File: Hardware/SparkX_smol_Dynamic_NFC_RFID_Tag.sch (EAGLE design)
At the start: 22 parts, among them U1 ST25DV64KC

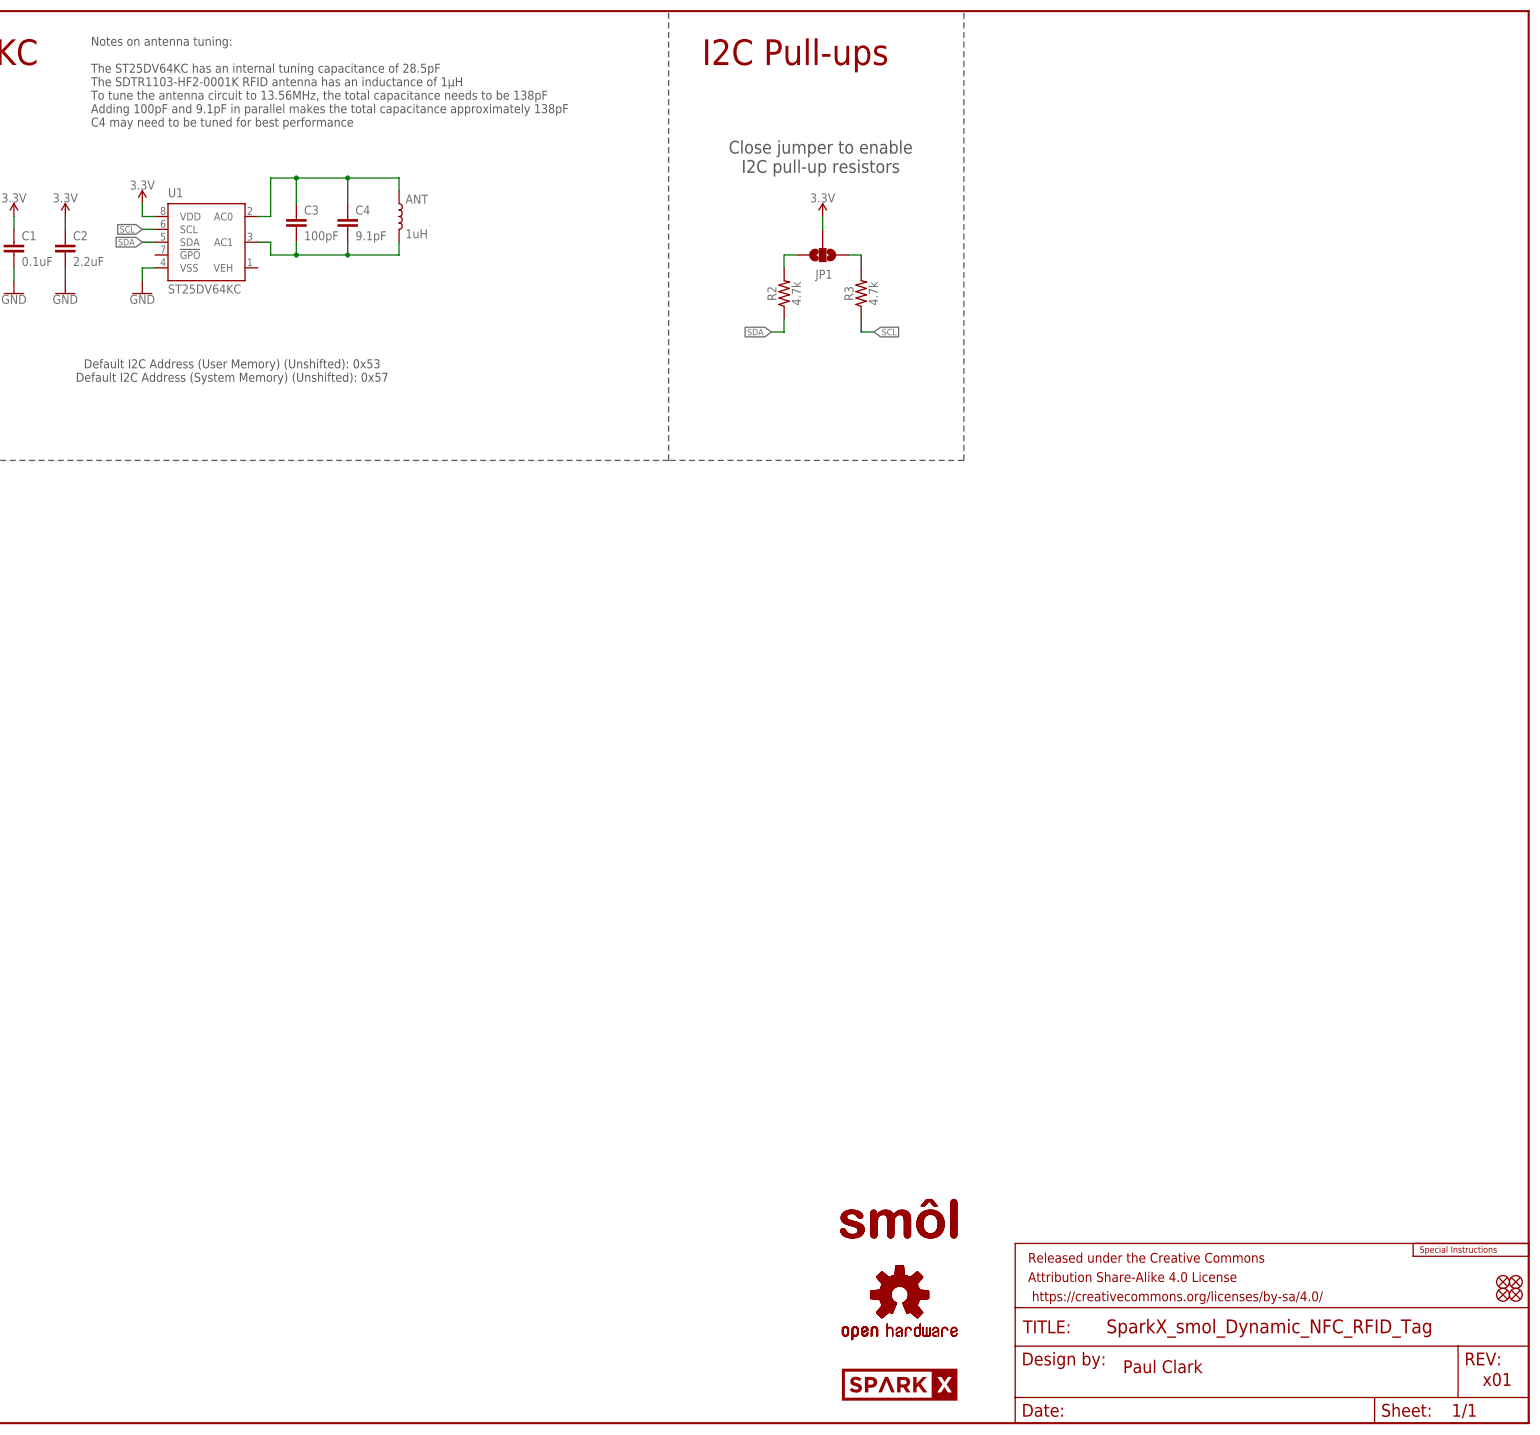
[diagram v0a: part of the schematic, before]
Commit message: x02: change to W3102 antenna
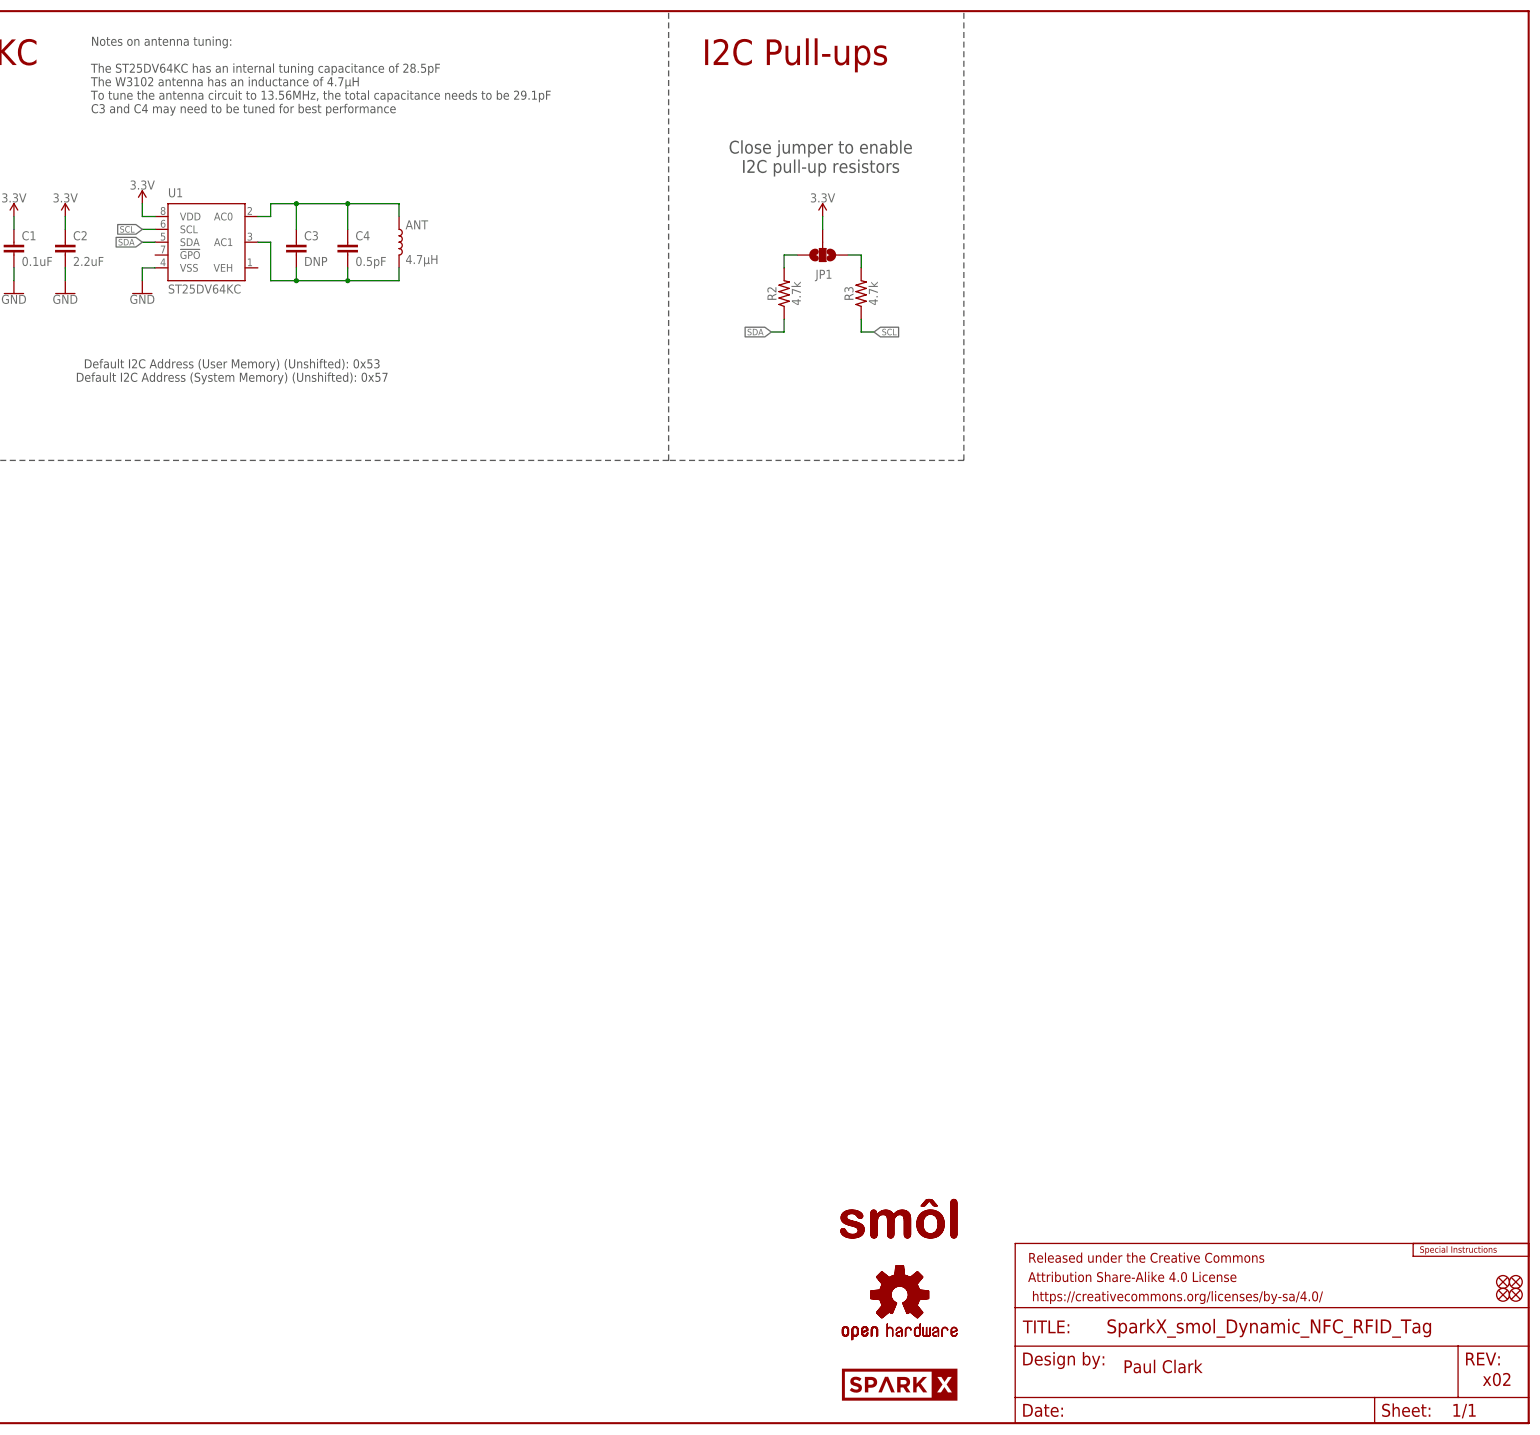
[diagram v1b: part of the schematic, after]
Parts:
- ANT: value 1uH -> 4.7μH; device SparkFun-RF:RFID_ANTENNA_SDTR1103-HF2-1UH -> SparkFun-RF:RFID_ANTENNA_W3102
- C3: value 100pF -> DNP; device SparkFun-Capacitors:100PF-0402T-50V-5% -> SparkFun-Capacitors:DNP-0402-TIGHT_NO_CREAM
- C4: value 9.1pF -> 0.5pF; device SparkFun-Capacitors:9.1PF-0402-TIGHT -> SparkFun-Capacitors:0.5PF-0402_TIGHT-50V-PM0.05PF-NP0
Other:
- note added: "Notes on antenna tuning: The ST25DV64KC has an internal tuning capacitance of 28.5pF The W3102 antenna has an inductance of 4.7µH To tune the antenna circuit to 13.56MHz, the total capacitance needs to be 29.1pF C3 and C4 may need to be tuned for best performance"
- note added: "x02"
- note removed: "Notes on antenna tuning: The ST25DV64KC has an internal tuning capacitance of 28.5pF The SDTR1103-HF2-0001K RFID antenna has an inductance of 1µH To tune the antenna circuit to 13.56MHz, the total capacitance needs to be 138pF Adding 100pF and 9.1pF in parallel makes the total capacitance approximately 138pF C4 may need to be tuned for best performance"
- note removed: "x01"
- moved on the sheet: ANT, C3, C4
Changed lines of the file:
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@@
 <part name="SUPPLY2" library="SparkFun-PowerSymbols" deviceset="3.3V" device=""/>
 <part name="GND2" library="SparkFun-PowerSymbols" deviceset="GND" device=""/>
-<part name="C3" library="SparkFun-Capacitors" deviceset="100PF" device="-0402T-50V-5%" value="100pF"/>
-<part name="C4" library="SparkFun-Capacitors" deviceset="9.1PF" device="-0402-TIGHT" value="9.1pF"/>
-<part name="ANT" library="SparkFun-RF" deviceset="RFID_ANTENNA_SDTR1103-HF2" device="-1UH" value="1uH"/>
+<part name="C3" library="SparkFun-Capacitors" deviceset="DNP" device="-0402-TIGHT_NO_CREAM" value="DNP"/>
+<part name="C4" library="SparkFun-Capacitors" deviceset="0.5PF" device="-0402_TIGHT-50V-PM0.05PF-NP0" value="0.5pF"/>
+<part name="ANT" library="SparkFun-RF" deviceset="RFID_ANTENNA_W3102" device="" value="4.7μH"/>
 <part name="R2" library="SparkFun-Resistors" deviceset="4.7KOHM" device="-0402T-1/16W-1%" value="4.7k"/>
 <part name="R3" library="SparkFun-Resistors" deviceset="4.7KOHM" device="-0402T-1/16W-1%" value="4.7k"/>
@@
 <plain>
 <text x="351.536" y="9.906" size="2.54" layer="94">Paul Clark</text>
-<text x="422.656" y="7.366" size="2.54" layer="94">x01</text>
+<text x="422.656" y="7.366" size="2.54" layer="94">x02</text>
 <wire x1="88.9" y1="190.5" x2="88.9" y2="279.4" width="0.2032" layer="97" style="longdash"/>
 <wire x1="88.9" y1="190.5" x2="0" y2="190.5" width="0.2032" layer="97" style="longdash"/>
@@
 <text x="147.32" y="274.32" size="1.778" layer="97" align="top-left">Notes on antenna tuning:
 The ST25DV64KC has an internal tuning capacitance of 28.5pF
-The SDTR1103-HF2-0001K RFID antenna has an inductance of 1µH
-To tune the antenna circuit to 13.56MHz, the total capacitance needs to be 138pF
-Adding 100pF and 9.1pF in parallel makes the total capacitance approximately 138pF
-C4 may need to be tuned for best performance</text>
+The W3102 antenna has an inductance of 4.7µH
+To tune the antenna circuit to 13.56MHz, the total capacitance needs to be 29.1pF
+C3 and C4 may need to be tuned for best performance</text>
 <text x="291.719" y="250.571" size="2.54" layer="97" font="vector" align="center">Close jumper to enable
 I2C pull-up resistors</text>
@@
 <attribute name="VALUE" x="132.08" y="223.266" size="1.778" layer="96" font="vector" align="top-center"/>
 </instance>
-<instance part="C3" gate="G$1" x="187.96" y="236.22" smashed="yes">
-<attribute name="NAME" x="189.484" y="239.141" size="1.778" layer="95" font="vector"/>
-<attribute name="VALUE" x="189.484" y="234.061" size="1.778" layer="96" font="vector"/>
-</instance>
-<instance part="C4" gate="G$1" x="198.12" y="236.22" smashed="yes">
-<attribute name="NAME" x="199.644" y="239.141" size="1.778" layer="95" font="vector"/>
-<attribute name="VALUE" x="199.644" y="234.061" size="1.778" layer="96" font="vector"/>
-</instance>
-<instance part="ANT" gate="G$1" x="208.28" y="238.76" smashed="yes">
-<attribute name="NAME" x="209.55" y="241.3" size="1.778" layer="95" font="vector"/>
-<attribute name="VALUE" x="209.55" y="236.22" size="1.778" layer="96" font="vector" align="top-left"/>
+<instance part="C3" gate="G$1" x="187.96" y="231.14" smashed="yes">
+<attribute name="NAME" x="189.484" y="234.061" size="1.778" layer="95" font="vector"/>
+<attribute name="VALUE" x="189.484" y="228.981" size="1.778" layer="96" font="vector"/>
+</instance>
+<instance part="C4" gate="G$1" x="198.12" y="231.14" smashed="yes">
+<attribute name="NAME" x="199.644" y="234.061" size="1.778" layer="95" font="vector"/>
+<attribute name="VALUE" x="199.644" y="228.981" size="1.778" layer="96" font="vector"/>
+</instance>
+<instance part="ANT" gate="G$1" x="208.28" y="233.68" smashed="yes">
+<attribute name="NAME" x="209.55" y="236.22" size="1.778" layer="95" font="vector"/>
+<attribute name="VALUE" x="209.55" y="231.14" size="1.778" layer="96" font="vector" align="top-left"/>
 </instance>
 <instance part="R2" gate="G$1" x="284.48" y="223.52" smashed="yes" rot="R90">
@@
 <pinref part="U1" gate="G$1" pin="AC1"/>
 <wire x1="180.34" y1="233.68" x2="182.88" y2="233.68" width="0.1524" layer="91"/>
-<wire x1="182.88" y1="233.68" x2="182.88" y2="231.14" width="0.1524" layer="91"/>
-<wire x1="182.88" y1="231.14" x2="187.96" y2="231.14" width="0.1524" layer="91"/>
+<wire x1="182.88" y1="233.68" x2="182.88" y2="226.06" width="0.1524" layer="91"/>
+<wire x1="182.88" y1="226.06" x2="187.96" y2="226.06" width="0.1524" layer="91"/>
 <pinref part="ANT" gate="G$1" pin="2"/>
-<wire x1="187.96" y1="231.14" x2="198.12" y2="231.14" width="0.1524" layer="91"/>
-<wire x1="198.12" y1="231.14" x2="208.28" y2="231.14" width="0.1524" layer="91"/>
-<wire x1="208.28" y1="231.14" x2="208.28" y2="233.68" width="0.1524" layer="91"/>
+<wire x1="187.96" y1="226.06" x2="198.12" y2="226.06" width="0.1524" layer="91"/>
+<wire x1="198.12" y1="226.06" x2="208.28" y2="226.06" width="0.1524" layer="91"/>
+<wire x1="208.28" y1="226.06" x2="208.28" y2="228.6" width="0.1524" layer="91"/>
 <pinref part="C4" gate="G$1" pin="2"/>
-<wire x1="198.12" y1="233.68" x2="198.12" y2="231.14" width="0.1524" layer="91"/>
-<junction x="198.12" y="231.14"/>
+<wire x1="198.12" y1="228.6" x2="198.12" y2="226.06" width="0.1524" layer="91"/>
+<junction x="198.12" y="226.06"/>
 <pinref part="C3" gate="G$1" pin="2"/>
-<wire x1="187.96" y1="233.68" x2="187.96" y2="231.14" width="0.1524" layer="91"/>
-<junction x="187.96" y="231.14"/>
+<wire x1="187.96" y1="228.6" x2="187.96" y2="226.06" width="0.1524" layer="91"/>
+<junction x="187.96" y="226.06"/>
 </segment>
 </net>
@@
 <pinref part="U1" gate="G$1" pin="AC0"/>
 <wire x1="180.34" y1="238.76" x2="182.88" y2="238.76" width="0.1524" layer="91"/>
-<wire x1="182.88" y1="238.76" x2="182.88" y2="246.38" width="0.1524" layer="91"/>
-<wire x1="182.88" y1="246.38" x2="187.96" y2="246.38" width="0.1524" layer="91"/>
+<wire x1="182.88" y1="238.76" x2="182.88" y2="241.3" width="0.1524" layer="91"/>
+<wire x1="182.88" y1="241.3" x2="187.96" y2="241.3" width="0.1524" layer="91"/>
 <pinref part="ANT" gate="G$1" pin="1"/>
-<wire x1="187.96" y1="246.38" x2="198.12" y2="246.38" width="0.1524" layer="91"/>
-<wire x1="198.12" y1="246.38" x2="208.28" y2="246.38" width="0.1524" layer="91"/>
-<wire x1="208.28" y1="246.38" x2="208.28" y2="243.84" width="0.1524" layer="91"/>
+<wire x1="187.96" y1="241.3" x2="198.12" y2="241.3" width="0.1524" layer="91"/>
+<wire x1="198.12" y1="241.3" x2="208.28" y2="241.3" width="0.1524" layer="91"/>
+<wire x1="208.28" y1="241.3" x2="208.28" y2="238.76" width="0.1524" layer="91"/>
 <pinref part="C4" gate="G$1" pin="1"/>
-<wire x1="198.12" y1="241.3" x2="198.12" y2="246.38" width="0.1524" layer="91"/>
-<junction x="198.12" y="246.38"/>
+<wire x1="198.12" y1="236.22" x2="198.12" y2="241.3" width="0.1524" layer="91"/>
+<junction x="198.12" y="241.3"/>
 <pinref part="C3" gate="G$1" pin="1"/>
-<wire x1="187.96" y1="241.3" x2="187.96" y2="246.38" width="0.1524" layer="91"/>
-<junction x="187.96" y="246.38"/>
-</segment>
-</net>
+<wire x1="187.96" y1="236.22" x2="187.96" y2="241.3" width="0.1524" layer="91"/>
+<junction x="187.96" y="241.3"/>
+</segment>
+</net>
